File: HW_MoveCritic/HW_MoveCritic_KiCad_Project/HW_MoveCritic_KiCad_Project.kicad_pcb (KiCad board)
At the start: 2 copper layers, 41 parts, among them J2 Conn_ARM_SWD_TagConnect_TC2030, J3 USB_C_Receptacle_USB2.0, SW1 SW_Push, U1 STM32WB55CEUx, U2 USBLC6-2P6, U3 MIC5365-3.3YD5, X1 32KHz768, X2 32MHz

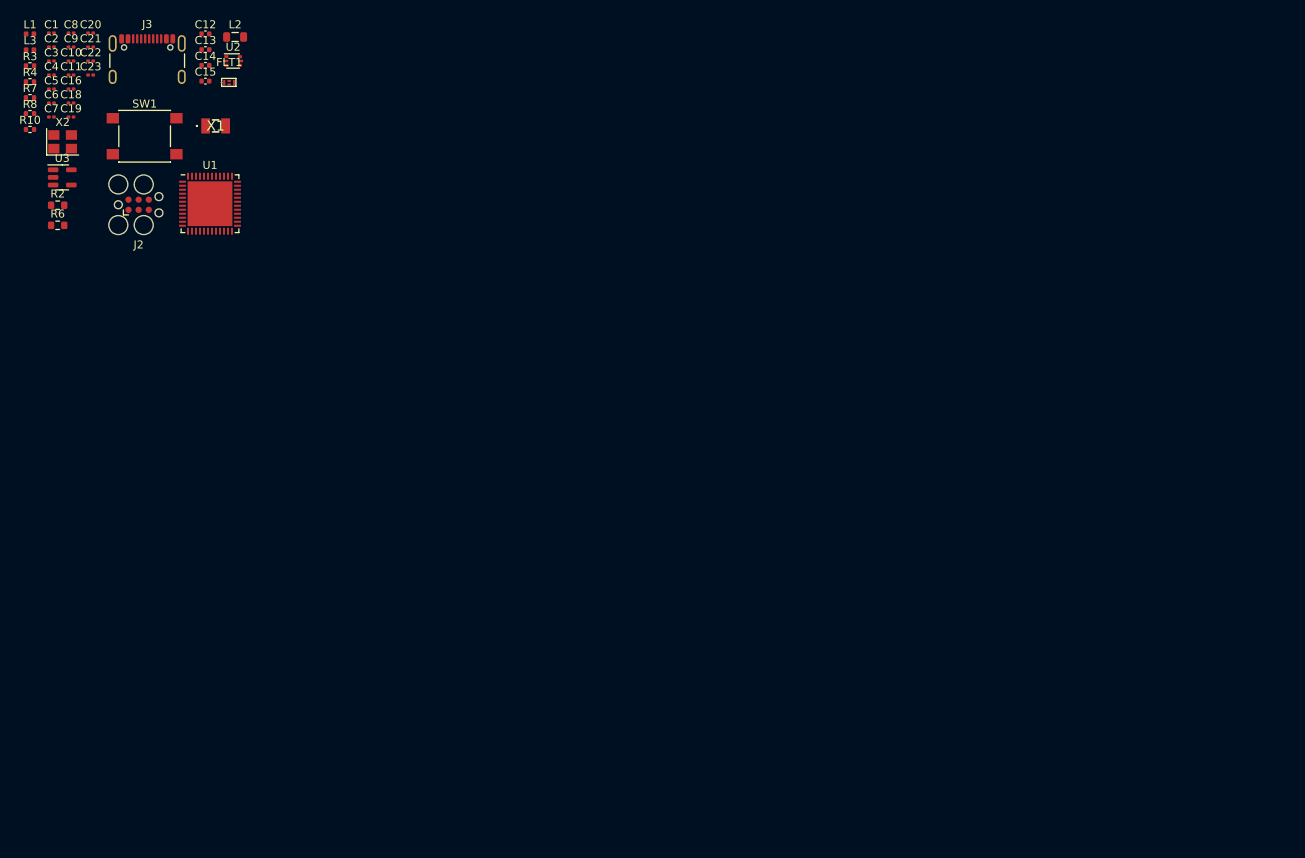
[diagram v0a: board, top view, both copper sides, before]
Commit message: V0.1 - Complete Schematic, layout incomplete
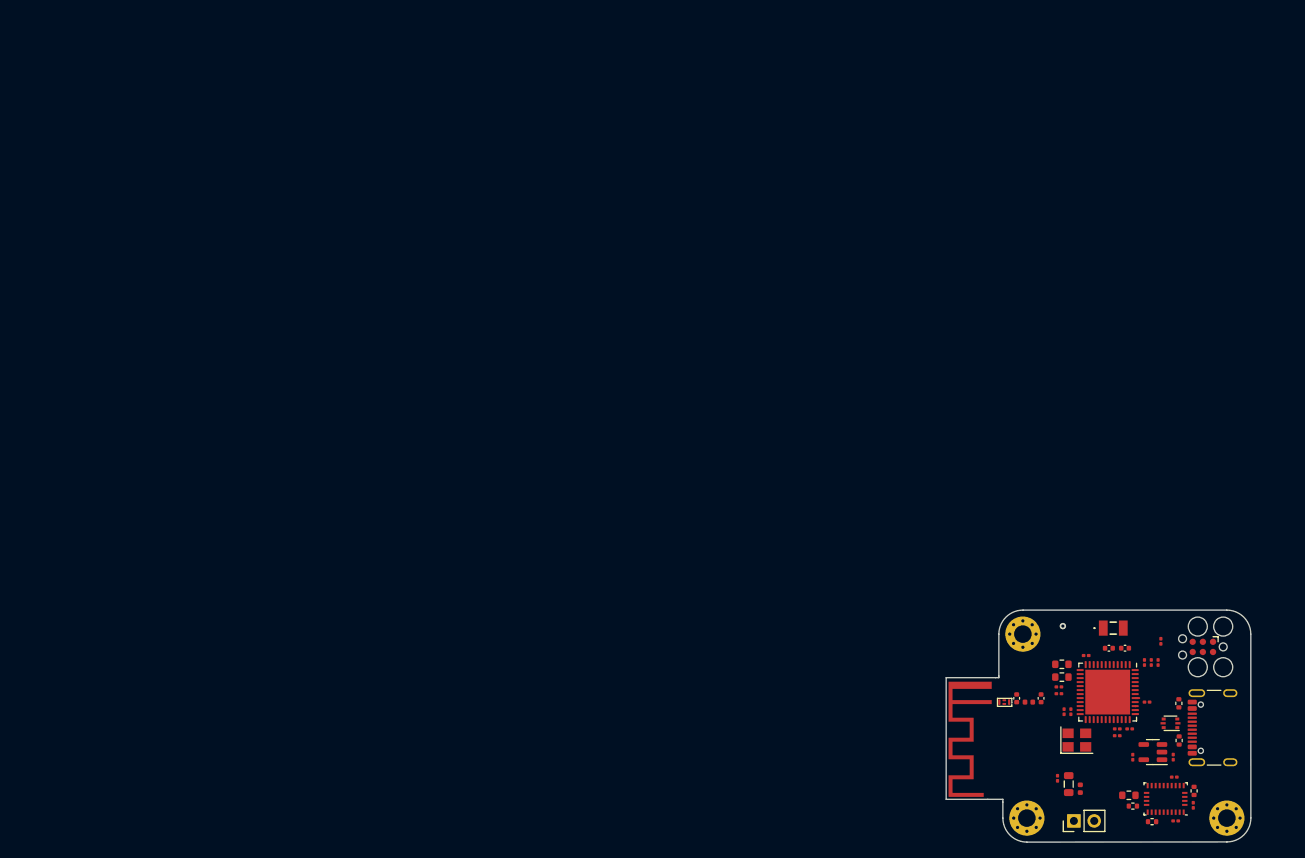
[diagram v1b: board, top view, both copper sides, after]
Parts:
- added AE1: Antenna_Chip, 830009678:2400MHz_PCB_Meander_Antenna, F.Cu at (135.1, 96.5)
- added C17: 4u7, Capacitor_SMD:C_0201_0603Metric, F.Cu at (144.0, 97.6)
- added H1: MountingHole, MountingHole:MountingHole_2.2mm_M2_Pad_Via, F.Cu at (139.5, 91.0)
- added H2: MountingHole, MountingHole:MountingHole_2.2mm_M2_Pad_Via, F.Cu at (140.0, 114.0)
- added H3: MountingHole, MountingHole:MountingHole_2.2mm_M2_Pad_Via, F.Cu at (165.0, 114.0)
- added R1: 1k, Resistor_SMD:R_0603_1608Metric, F.Cu at (144.4, 94.8)
- added U5: BNO086, Package_LGA:LGA-28_5.2x3.8mm_P0.5mm, F.Cu at (157.3, 111.6)
- C16: value 100n -> 4u7
- SW1: footprint Button_Switch_SMD:SW_Push_1P1T_NO_6x6mm_H9.5mm -> Connector_PinHeader_2.54mm:PinHeader_1x02_P2.54mm_Vertical
- moved C20 167.6 mm to (158.6, 114.3), turned to 180 degrees
- moved R10 167.4 mm to (160.9, 110.6), turned to -90 degrees
- moved C21 167.3 mm to (160.8, 112.4), turned to -90 degrees
- moved R8 165.9 mm to (155.7, 114.5), turned to 180 degrees
- moved R4 165.6 mm to (159.0, 104.3), turned to -90 degrees
- moved R3 164.2 mm to (159.0, 99.7), turned to 90 degrees
- moved R7 163.9 mm to (153.2, 112.5)
- moved C22 162.4 mm to (158.4, 108.9)
- moved L1 161.7 mm to (146.7, 110.3), turned to -90 degrees
- moved C18 160.2 mm to (158.3, 106.4), turned to 90 degrees
- moved C3 158.7 mm to (155.0, 99.5)
- moved C4 157.6 mm to (152.8, 102.8)
- moved J3 157.6 mm to (164.3, 102.7), turned to 90 degrees
- moved C8 157.1 mm to (151.3, 102.8), turned to 180 degrees
- moved C9 156.6 mm to (151.3, 103.7), turned to 180 degrees
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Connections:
- net Net-(J2-SWO) renamed /SWO
- C1 pad 1: BNO_BOOTN -> +3.3V
- C1 pad 2: NRST -> GND
- C10 pad 1: BNO_BOOTN -> +3.3V
- C10 pad 2: NRST -> GND
- C11 pad 2: NRST -> GND
- C12 pad 2: NRST -> GND
- C13 pad 2: NRST -> GND
- C14 pad 2: NRST -> GND
- C15 pad 1: Net-(C15-Pad1) -> Net-(FLT1-IN)
- C15 pad 2: NRST -> GND
- C16 pad 1: Net-(U1-NRST) -> NRST
- C16 pad 2: NRST -> GND
- C18 pad 2: NRST -> GND
- C19 pad 1: BNO_BOOTN -> +3.3V
- C19 pad 2: NRST -> GND
- C2 pad 1: BNO_BOOTN -> +3.3V
- C2 pad 2: NRST -> GND
- C20 pad 1: BNO_BOOTN -> +3.3V
- C20 pad 2: NRST -> GND
- C21 pad 1: BNO_BOOTN -> +3.3V
- C21 pad 2: NRST -> GND
- C22 pad 2: NRST -> GND
- C23 pad 1: BNO_BOOTN -> +3.3V
- C23 pad 2: NRST -> GND
- C3 pad 1: BNO_BOOTN -> +3.3V
- C3 pad 2: NRST -> GND
- C4 pad 1: BNO_BOOTN -> +3.3V
- C4 pad 2: NRST -> GND
- C5 pad 1: BNO_BOOTN -> +3.3V
- C5 pad 2: NRST -> GND
- C6 pad 1: BNO_BOOTN -> +3.3V
- C6 pad 2: NRST -> GND
- C7 pad 1: BNO_BOOTN -> +3.3V
- C7 pad 2: NRST -> GND
- C8 pad 1: BNO_BOOTN -> +3.3V
- C8 pad 2: NRST -> GND
- C9 pad 1: BNO_BOOTN -> +3.3V
- C9 pad 2: NRST -> GND
- FLT1 pad 1: (no net) -> Net-(FLT1-IN)
- FLT1 pad 2: (no net) -> GND
- FLT1 pad 3: (no net) -> /RF_ANT
- J2 pad 1: BNO_BOOTN -> +3.3V
- J2 pad 2: Net-(J2-SWDIO) -> /SWDIO
- J2 pad 4: Net-(J2-SWCLK) -> /SWCLK
- J2 pad 5: NRST -> GND
- J3 pad A1: NRST -> GND
- J3 pad A12: NRST -> GND
- J3 pad B1: NRST -> GND
- J3 pad B12: NRST -> GND
- J3 pad S1: NRST -> GND
- L3 pad 2: Net-(C15-Pad1) -> Net-(FLT1-IN)
- R10 pad 1: Net-(U5-~{BOOT}) -> +3.3V
- R10 pad 2: BNO_BOOTN -> BNO_NBOOT
- R2 pad 1: NRST -> GND
- R3 pad 2: NRST -> GND
- R4 pad 2: NRST -> GND
- R6 pad 1: NRST -> GND
- R6 pad 2: BNO_BOOTN -> +3.3V
- R7 pad 1: BNO_BOOTN -> +3.3V
- R8 pad 1: BNO_BOOTN -> +3.3V
- SW1 pad 1: /BOOT_0 -> Net-(R1-Pad1)
- SW1 pad 2: BNO_BOOTN -> +3.3V
- U1 pad 1: BNO_BOOTN -> +3.3V
- U1 pad 10: BNO_BOOTN -> unconnected-(U1-PA1-Pad10)
- U1 pad 11: BNO_NRST -> unconnected-(U1-PA2-Pad11)
- U1 pad 12: BNO_NINT -> unconnected-(U1-PA3-Pad12)
- U1 pad 18: unconnected-(U1-PA9-Pad18) -> I2C1_SCL
- U1 pad 20: BNO_BOOTN -> +3.3V
- U1 pad 22: NRST -> GND
- U1 pad 23: BNO_BOOTN -> +3.3V
- U1 pad 32: NRST -> GND
- U1 pad 34: BNO_BOOTN -> +3.3V
- U1 pad 35: BNO_BOOTN -> +3.3V
- U1 pad 36: unconnected-(U1-PA10-Pad36) -> I2C1_SDA
- U1 pad 39: Net-(J2-SWDIO) -> /SWCLK
- U1 pad 40: BNO_BOOTN -> +3.3V
- U1 pad 41: Net-(J2-SWCLK) -> /SWDIO
- U1 pad 45: unconnected-(U1-PB5-Pad45) -> BNO_NINT
- U1 pad 46: unconnected-(U1-PB6-Pad46) -> BNO_NRST
- U1 pad 47: unconnected-(U1-PB7-Pad47) -> BNO_NBOOT
- U1 pad 48: BNO_BOOTN -> +3.3V
- U1 pad 49: NRST -> GND
- U1 pad 5: I2C1_SCL -> unconnected-(U1-PB8-Pad5)
- U1 pad 6: I2C1_SDA -> unconnected-(U1-PB9-Pad6)
- U1 pad 7: Net-(U1-NRST) -> NRST
- U1 pad 8: BNO_BOOTN -> +3.3V
- U2 pad 2: NRST -> GND
- U3 pad 2: NRST -> GND
- U3 pad 5: BNO_BOOTN -> +3.3V
- X2 pad 2: NRST -> GND
- X2 pad 4: NRST -> GND
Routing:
- net /SWDIO: track 0.00 -> 0.51 mm
- net GND: vias 0 -> 1
- added copper zone on In1.Cu, net GND
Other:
- board outline added: 32.9 x 29 mm
- copper layers 2 -> 4
- rule pad_to_mask_clearance: 0 -> 0.08

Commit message: Large Commit for HW design
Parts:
- removed H3: MountingHole, MountingHole:MountingHole_2.2mm_M2_Pad_Via
- added D1: B5819W, Diode_SMD:D_SOD-123, F.Cu at (136.2, 91.7)
- added D2: LED, LED_SMD:LED_0402_1005Metric, F.Cu at (150.2, 76.2)
- added FID1: Fiducial, Fiducial:Fiducial_1mm_Mask2mm, F.Cu at (159.3, 76.1)
- added FID2: Fiducial, Fiducial:Fiducial_1mm_Mask2mm, F.Cu at (161.5, 100.5)
- added FID3: Fiducial, Fiducial:Fiducial_1mm_Mask2mm, F.Cu at (139.6, 76.0)
- added H4: MountingHole, MountingHole:MountingHole_2.2mm_M2_DIN965, F.Cu at (164.2, 99.3)
- added J1: JST_PH_2.00mm, Connector_JST:JST_PH_B2B-PH-K_1x02_P2.00mm_Vertical, F.Cu at (136.9, 95.5)
- added R5: 220R, Resistor_SMD:R_0201_0603Metric, F.Cu at (148.7, 76.5)
- AE1: footprint 830009678:2400MHz_PCB_Meander_Antenna -> 830009678:2400MHz_PCB_Inverted_F
- C1, C10, C2, C3, C4, C5, C6, C8: value 100n -> 0u1
- H1, H2: footprint MountingHole:MountingHole_2.2mm_M2_Pad_Via -> MountingHole:MountingHole_2.2mm_M2_DIN965
- U1: value STM32WB55CEUx -> STM32WB55CEU6
- moved AE1 38.5 mm to (172.8, 88.7)
- moved H2 36.9 mm to (136.2, 77.3), turned to -90 degrees
- moved C18 33.2 mm to (141.8, 77.6), turned to -90 degrees
- moved J3 32.8 mm to (136.8, 84.9), turned to -90 degrees
- moved L2 32.3 mm to (151.7, 78.2), turned to 0 degrees
- moved FLT1 31.4 mm to (164.6, 84.2), turned to 0 degrees
- moved L1 30.4 mm to (151.1, 80.3), turned to 90 degrees
- moved U3 29.8 mm to (144.3, 78.2), turned to 0 degrees
- moved C19 29.5 mm to (146.8, 77.6), turned to -90 degrees
- moved C11 29.4 mm to (152.4, 80.9), turned to 0 degrees
- moved C15 28.3 mm to (163.1, 84.7), turned to -90 degrees
- moved H1 28.2 mm to (164.2, 77.3), turned to -90 degrees
- moved R4 27.6 mm to (142.1, 82.6), turned to 90 degrees
- moved X2 26.7 mm to (156.2, 79.5), turned to 180 degrees
- moved L3 26.2 mm to (161.6, 84.2), turned to 0 degrees
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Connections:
- net Net-(U2-VBUS) renamed +5V
- U1 pad 12: unconnected-(U1-PA3-Pad12) -> Net-(D2-A)
- U1 pad 13: unconnected-(U1-PA4-Pad13) -> BNO_NBOOT
- U1 pad 14: unconnected-(U1-PA5-Pad14) -> BNO_NRST
- U1 pad 15: unconnected-(U1-PA6-Pad15) -> BNO_NINT
- U1 pad 45: BNO_NINT -> unconnected-(U1-PB5-Pad45)
- U1 pad 46: BNO_NRST -> unconnected-(U1-PB6-Pad46)
- U1 pad 47: BNO_NBOOT -> unconnected-(U1-PB7-Pad47)
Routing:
- net GND: track 0.00 -> 31.1 mm, vias 1 -> 89
- net +3.3V: track 0.00 -> 27.3 mm, vias 0 -> 22
- net BNO_NBOOT: track 0.00 -> 20.6 mm
- net I2C1_SDA: track 0.00 -> 20.4 mm, vias 0 -> 2
- net /SWDIO: track 0.51 -> 20.1 mm
- net Net-(D2-A): track 0.00 -> 18.7 mm, vias 0 -> 2
- net /SWCLK: track 0.35 -> 16.9 mm, vias 0 -> 2
- net /BOOT_0: track 0.00 -> 16.0 mm, vias 0 -> 2
- net NRST: track 0.04 -> 15.3 mm, vias 0 -> 2
- net /SWO: track 0.00 -> 15.0 mm
- net BNO_NINT: track 0.00 -> 12.0 mm, vias 0 -> 2
- net BNO_NRST: track 0.00 -> 10.1 mm, vias 0 -> 2
- net I2C1_SCL: track 0.00 -> 7.89 mm
- net /LSE_OUT: track 0.00 -> 6.05 mm
- net RF1: track 0.00 -> 5.74 mm
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- added copper zone on B.Cu, net +3.3V
- added copper zone on F.Cu, net +3.3V
- added copper zone on B.Cu, net +5V
- added copper zone on F.Cu, net +5V
- added copper zone on F.Cu, net /SMPSFB
- added copper zone on F.Cu, net /VIN
- added copper zone on F.Cu, net GND
- added copper zone on In2.Cu, net GND
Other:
- board size 32.9 x 29 mm -> 34 x 27.7 mm
- rule pad_to_mask_clearance: 0.08 -> 0
- board text added: "MoveCritic FBTM REV A AC 03/24"
- board text added: "X"
- board text added: "Y"
